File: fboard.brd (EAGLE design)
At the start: 48.2 x 60.6 mm, 41 parts, among them U1 ATMEGA328PB-AU, U2 MPU-6050

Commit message: fixed schematic
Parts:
- removed C8: 0.1uF, rcl:C0805
- removed R12: 330R, rcl:R0805
- removed R13: 2.7kR, rcl:R0805
- removed R14, R15: 4.7kR, rcl:R0805
- removed U$1: SS14, SS14:DO-214AC
- removed U$2: SK-3296S-01-L1, CustomParts:SK-3296S-01-L1
- removed U$3: RK-2032, CustomParts:RK-2032
- added BAT1: RK-2032, CustomParts:RK-2032
- added D1: MBR0520LT, diode:SOD123
- added Q1: SL2305, SL2305:SOT95P240X115-3N
- added S1: SK-3296S-01-L1, CustomParts:SK-3296S-01-L1
- added U3: SN74HC138PW, SN74HC138PW:SOP65P640X120-16N
- C5: value 0.1uF -> 10nF
- C6: value 10nF -> 2nF
- C7: value 2nF -> 0.1uF
- R10, R11: value 330R -> 4.7kR
- moved U$6 95.2 mm to (2.54, 2.54)
- moved R8 67.5 mm to (61.0, 3.81)
- moved LED8 65.6 mm to (61.0, 8.89), turned to 0 degrees
- moved C5 64.8 mm to (63.5, 39.4), turned to 0 degrees
- moved R7 60.2 mm to (55.9, 3.81)
- moved C2 57.3 mm to (43.2, 38.1)
- moved LED7 57.1 mm to (55.9, 8.89), turned to 0 degrees
- moved R9 56.9 mm to (40.6, 3.81)
- moved U2 54.0 mm to (58.4, 41.9), turned to 90 degrees
- moved R6 53.9 mm to (50.8, 3.81)
- moved C4 52.1 mm to (63.5, 43.2)
- moved U$5 51.4 mm to (66.0, 49.5)
- moved R1 51.2 mm to (20.3, 3.81), turned to 90 degrees
- moved C6 50.8 mm to (53.3, 44.5)
- moved C7 50.1 mm to (40.6, 38.1), turned to 270 degrees
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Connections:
- removed net B3: ISP1.4, R10.1
- removed net B4: ISP1.1, R11.2
- removed net B5: ISP1.3, R12.2
- removed net N$10: LED4.A, R4.2
- removed net N$11: LED9.A, R5.2
- removed net N$12: LED5.A, R6.2
- removed net N$13: LED6.A, R7.2
- removed net N$14: LED7.A, R8.2
- removed net N$15: LED8.A, R9.2
- removed net N$16: U$1.C, U$2.P3
- removed net N$2: LED1.A, R1.2
- removed net PB0: R6.1, U1.12
- removed net PB1: R5.1, U1.13
- removed net PB2: R4.1, U1.14
- removed net VOLTAGEPROTEC: U$1.A, U$3.P$1, U$3.P$2
- new net 3V_INPUT: BAT1.P$1, BAT1.P$2, D1.A, ISP1.2, Q1.3
- new net N$1: LED2.A, R2.1
- new net N$19: LED1.C, R1.2
- new net N$3: LED3.A, R3.1
- new net N$4: LED4.A, R4.1
- new net N$5: LED9.A, R9.1
- new net N$6: LED5.A, R5.1
- new net N$7: LED6.A, R6.1
- new net PB6: LED1.A, U1.7
- new net PB7: U1.8, U3.6
- new net VPROTEC: D1.C, Q1.2, S1.P1
- new net Y0: LED8.C, U3.15
- new net Y1: LED7.C, U3.14
- new net Y2: LED6.C, U3.13
- new net Y3: LED5.C, U3.12
- new net Y4: LED9.C, U3.11
- new net Y5: LED4.C, U3.10
- new net Y6: LED3.C, U3.9
- new net Y7: LED2.C, U3.7
- net CPOUT: now also C6.1; no longer C7.1
- net GND: now also BAT1.P$3, C3.2, C4.2, C6.2, C7.1, Q1.1, R1.1, S1.P3, U3.8; no longer C3.1, C4.1, C6.1, C7.2, C8.1, LED1.C, LED2.C, LED3.C, LED4.C, LED5.C, LED6.C, LED7.C, LED8.C, LED9.C, U$3.P$3
- net N$8: now also LED7.A, R7.1; no longer LED2.A, R2.2
- net N$9: now also LED8.A, R8.1; no longer LED3.A, R3.2
- net PB3: now also ISP1.4; no longer R10.2, R3.1
- net PB4: now also ISP1.1; no longer R11.1, R2.1
- net PB5: now also ISP1.3; no longer R1.1, R12.1
- net PC4: now also R11.1; no longer R15.2
- net PC5: now also R10.1; no longer R14.2
- net PC6: no longer R13.2
- net PD5: now also U3.3; no longer R9.1
- net PD6: now also U3.2; no longer R8.1
- net PD7: now also U3.1; no longer R7.1
- net REGOUT: now also C4.1; no longer C5.1
- net VCC: now also C3.1, C5.1, C7.2, R10.2, R11.2, R2.2, R3.2, R4.2, R5.2, R6.2, R7.2, R8.2, R9.2, S1.P2, U3.16; no longer C3.2, C4.2, C6.2, C8.2, ISP1.2, R13.1, R14.1, R15.1, U$2.P1
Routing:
- net 3V_INPUT: track 0.00 -> 73.6 mm
- net VCC: track 139.0 -> 207.5 mm
- net VOLTAGEPROTEC: track 40.1 -> 0.00 mm
- net Y6: track 0.00 -> 36.7 mm
- net Y5: track 0.00 -> 35.4 mm
- net Y4: track 0.00 -> 33.6 mm
- net Y3: track 0.00 -> 33.6 mm
- net PB6: track 0.00 -> 32.7 mm
- net Y7: track 0.00 -> 31.1 mm
- net Y2: track 0.00 -> 29.9 mm
- net PD5: track 34.7 -> 5.66 mm
- net Y1: track 0.00 -> 27.6 mm
- net Y0: track 0.00 -> 25.3 mm
- net B3: track 25.3 -> 0.00 mm, vias 2 -> 0
- net PD6: track 30.7 -> 5.73 mm
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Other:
- board size 48.2 x 60.6 mm -> 68.6 x 51.7 mm

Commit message: fixed more stuff
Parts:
- BAT1: device CustomParts:RK-2032 -> ECE_388_CustomParts_V1.1:RK-2032
- D1: value MBR0520LT -> SCHOTTKY_SS14L; device diode:SOD123 -> ECE_388_CustomParts_V1.1:SOD123FL
- S1: device CustomParts:SK-3296S-01-L1 -> ECE_388_CustomParts_V1.1:SK-3296S-01-L1
- moved U$4 79.0 mm to (66.0, 2.54)
- moved U$5 63.5 mm to (2.54, 49.5)
- moved D1 1.80 mm to (10.2, 19.1)
- moved BAT1 1.27 mm to (6.35, 48.3)
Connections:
- net 3V_INPUT renamed BAT_3V
- net PB3 renamed MOSI
- net PB4 renamed MISO
- net PB5 renamed SCK
- net PB6 renamed PB6_LED1
- net PB7 renamed D_EN
- net PC4 renamed SDA0
- net PC5 renamed SCL0
- net PC6 renamed RST
- net PD5 renamed D_INPUT_C
- net PD6 renamed D_INPUT_B
- net PD7 renamed D_INPUT_A
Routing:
- net VPROTEC: track 20.7 -> 16.8 mm
- net BAT_3V: track 73.6 -> 75.7 mm
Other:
- board text added: "( ͡° ͜ʖ ͡°)"
- board text added: "11/9/20"
- board text added: "Digital Level V2"
- board text added: "Michael Bourgeois"
- board text added: "https://github.com/mbourgeois2/ECE-388-Digital-Level-Design-Project"

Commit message: updated stuff
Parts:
- removed D1: SCHOTTKY_SS14L, ECE_388_CustomParts_V1.1:SOD123FL
- removed S1: SK-3296S-01-L1, ECE_388_CustomParts_V1.1:SK-3296S-01-L1
- moved Q1 5.08 mm to (10.2, 19.1)
- moved C1 2.84 mm to (57.1, 48.3), turned to 180 degrees
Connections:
- removed net BAT_3V: BAT1.P$1, BAT1.P$2, D1.A, ISP1.2, Q1.3
- removed net VPROTEC: D1.C, Q1.2, S1.P1
- new net +3V3: C1.1, C2.1, C3.1, C5.1, C7.2, Q1.2, R10.2, R11.2, R2.2, R3.2, R4.2, R5.2, R6.2, R7.2, R8.2, R9.2, U1.18, U1.20, U1.4, U2.13, U2.8, U3.16
- net GND: no longer S1.P3
- net VCC: now also BAT1.P$1, BAT1.P$2, ISP1.2, Q1.3; no longer C1.1, C2.1, C3.1, C5.1, C7.2, R10.2, R11.2, R2.2, R3.2, R4.2, R5.2, R6.2, R7.2, R8.2, R9.2, S1.P2, U1.18, U1.20, U1.4, U2.13, U2.8, U3.16
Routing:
- net +3V3: track 0.00 -> 201.5 mm
- net VCC: track 207.5 -> 68.8 mm
- net BAT_3V: track 75.7 -> 0.00 mm
- net VPROTEC: track 16.8 -> 0.00 mm
- net PB6_LED1: track 32.7 -> 30.5 mm

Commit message: board stuff
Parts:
- removed R10, R11: 4.7kR, rcl:R0805
- removed R5, R6, R7, R8, R9: 330R, rcl:R0805
- R2, R3, R4: value 330R -> 4.7kR
- moved R4 36.9 mm to (36.8, 40.6)
- moved R2 32.4 mm to (31.8, 35.6), turned to 90 degrees
- moved R3 32.4 mm to (36.8, 35.6), turned to 90 degrees
- moved Q1 13.3 mm to (22.9, 15.2)
- moved BAT1 9.25 mm to (15.2, 45.7)
- moved U$5 7.62 mm to (10.2, 49.5)
- moved U$6 7.62 mm to (10.2, 2.54)
- moved C3 7.41 mm to (39.4, 17.8), turned to 270 degrees
- moved LED6 6.84 mm to (53.3, 2.54)
- moved LED2 6.84 mm to (27.9, 2.54)
- moved LED3 6.84 mm to (33.0, 2.54)
- moved LED1 6.84 mm to (22.9, 2.54), turned to 0 degrees
- moved LED4 6.84 mm to (38.1, 2.54)
- moved LED5 6.84 mm to (48.3, 2.54)
- moved LED7 6.84 mm to (58.4, 2.54)
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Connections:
- net CPOUT renamed N$2
- net REGOUT renamed N$1
- removed net N$1 (its old number): LED2.A, R2.1
- removed net N$19: LED1.C, R1.2
- removed net N$3: LED3.A, R3.1
- removed net N$4: LED4.A, R4.1
- removed net N$5: LED9.A, R9.1
- removed net N$6: LED5.A, R5.1
- removed net N$7: LED6.A, R6.1
- removed net N$8: LED7.A, R7.1
- removed net N$9: LED8.A, R8.1
- removed net VCC: BAT1.P$1, BAT1.P$2, ISP1.2, Q1.3
- new net LED_LINE: LED1.A, LED2.A, LED3.A, LED4.A, LED5.A, LED6.A, LED7.A, LED8.A, LED9.A, R1.1
- new net N$12: BAT1.P$1, BAT1.P$2, Q1.3
- net +3V3: now also C7.1, ISP1.2, R1.2; no longer C7.2, R10.2, R11.2, R5.2, R6.2, R7.2, R8.2, R9.2
- net GND: now also C7.2; no longer C7.1, R1.1
- net PB6_LED1: now also LED1.C; no longer LED1.A
- net RST: now also R4.1
- net SCL0: now also R2.1; no longer R10.1
- net SDA0: now also R3.1; no longer R11.1
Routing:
- net VCC: track 68.8 -> 0.00 mm
- net +3V3: track 201.5 -> 142.8 mm, vias 0 -> 2
- net LED_LINE: track 0.00 -> 44.5 mm
- net N$12: track 0.00 -> 34.0 mm
- net Y0: track 25.3 -> 30.6 mm
- net Y6: track 36.7 -> 41.3 mm
- net Y7: track 31.1 -> 35.0 mm
- net Y5: track 35.4 -> 39.0 mm
- net N$9: track 3.08 -> 0.00 mm
- net N$8: track 3.08 -> 0.00 mm
- net N$7: track 3.08 -> 0.00 mm
- net N$6: track 3.08 -> 0.00 mm
- net N$5: track 3.08 -> 0.00 mm
- net N$4: track 3.08 -> 0.00 mm
- net N$3: track 3.08 -> 0.00 mm
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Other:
- board size 68.6 x 51.7 mm -> 60.9 x 51.7 mm
- board text added: "11/10/20"
- board text removed: "11/9/20"

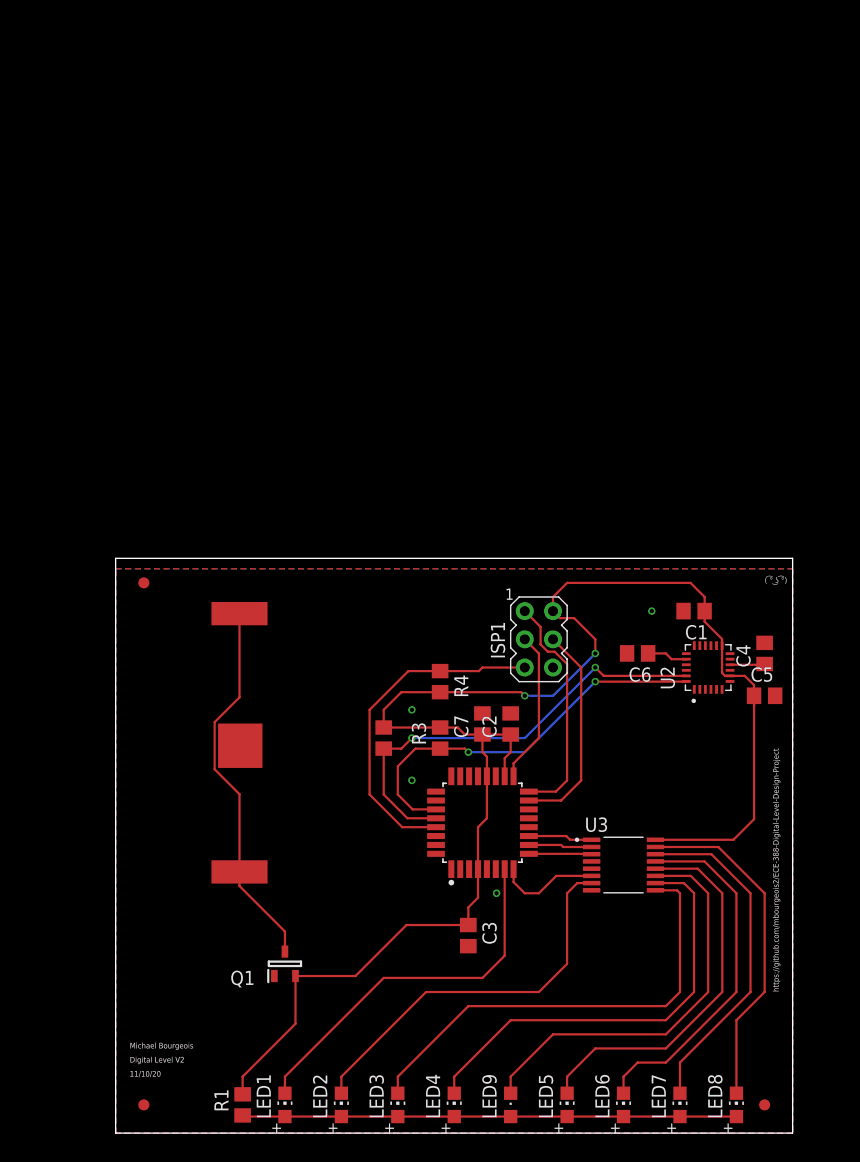
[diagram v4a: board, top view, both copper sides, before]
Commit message: moved a capacitor to reduce noise for pullups
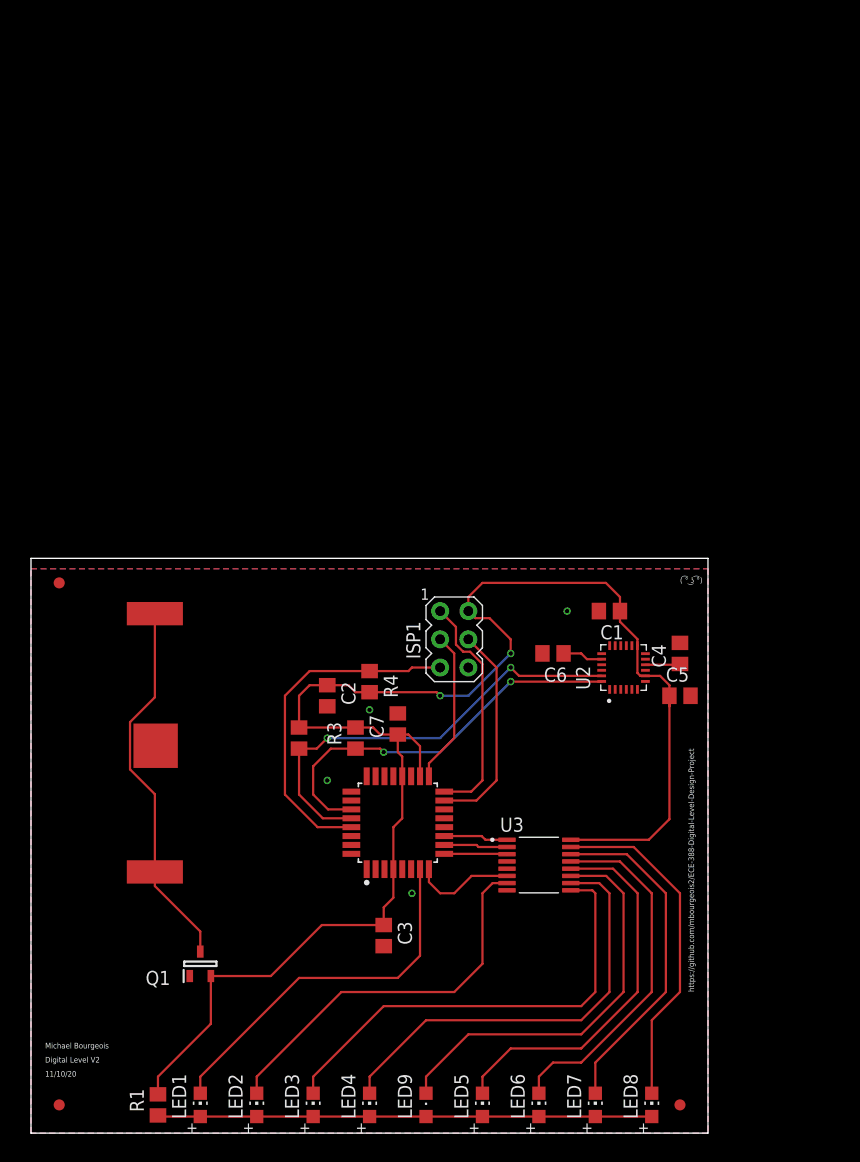
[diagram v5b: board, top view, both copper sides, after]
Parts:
- moved C2 16.7 mm to (26.7, 39.4), turned to 270 degrees
- moved C4 7.62 mm to (58.4, 43.2)
- moved C5 7.62 mm to (58.4, 39.4)
- moved LED3 7.62 mm to (25.4, 2.54)
- moved LED6 7.62 mm to (45.7, 2.54)
- moved LED7 7.62 mm to (50.8, 2.54)
- moved U$4 7.62 mm to (58.4, 2.54)
- moved U3 7.62 mm to (45.7, 24.1)
- moved LED2 7.62 mm to (20.3, 2.54)
- moved LED4 7.62 mm to (30.5, 2.54)
- moved R1 7.62 mm to (11.4, 2.54)
- moved R2 7.62 mm to (24.1, 35.6)
- moved BAT1 7.62 mm to (7.62, 45.7)
- moved U$5 7.62 mm to (2.54, 49.5)
- moved U$6 7.62 mm to (2.54, 2.54)
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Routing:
- net RST: track 30.4 -> 31.1 mm

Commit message: board stuff
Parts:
- moved C1 1.27 mm to (53.3, 47.0)
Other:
- board text added: "11/11/20"
- board text removed: "11/10/20"

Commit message: thicc power traces
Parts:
- moved C5 3.59 mm to (55.9, 36.8), turned to 180 degrees
- moved C4 2.84 mm to (55.9, 44.5)
- moved BAT1 2.54 mm to (7.62, 48.3)
- moved C1 1.27 mm to (52.1, 47.0)
- moved C6 1.27 mm to (45.7, 43.2)
- moved U2 1.27 mm to (52.1, 41.9)
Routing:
- net +3V3: track 142.7 -> 154.0 mm
- net N$12: track 34.0 -> 37.6 mm
- net SDA0: track 35.9 -> 34.7 mm
- net SCL0: track 40.3 -> 39.0 mm
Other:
- board text removed: "( ͡° ͜ʖ ͡°)"
